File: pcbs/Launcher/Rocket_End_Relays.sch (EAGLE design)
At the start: 40 parts, among them IC2 LM2576T-ADJ, K4 LD105, K5 LD105, K6 LD105, K7 LD105, T1 BC547, T2 BC547, T3 BC547, T4 BC547, T5 BC547, U1 ARDUINO-MEGAPRO-5V, X1 1751248, X2 22-23-2041, X3 22-23-2021, X4 1751248, X5 22-23-2021

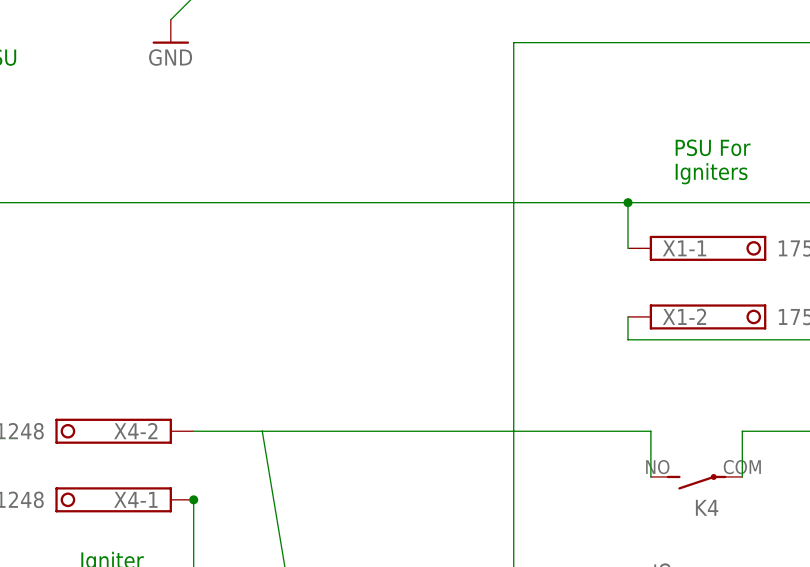
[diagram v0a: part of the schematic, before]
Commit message: * Moving relays in line a bit more * Added additional connector for Igniter battery, to give us more options * Rotated plugs
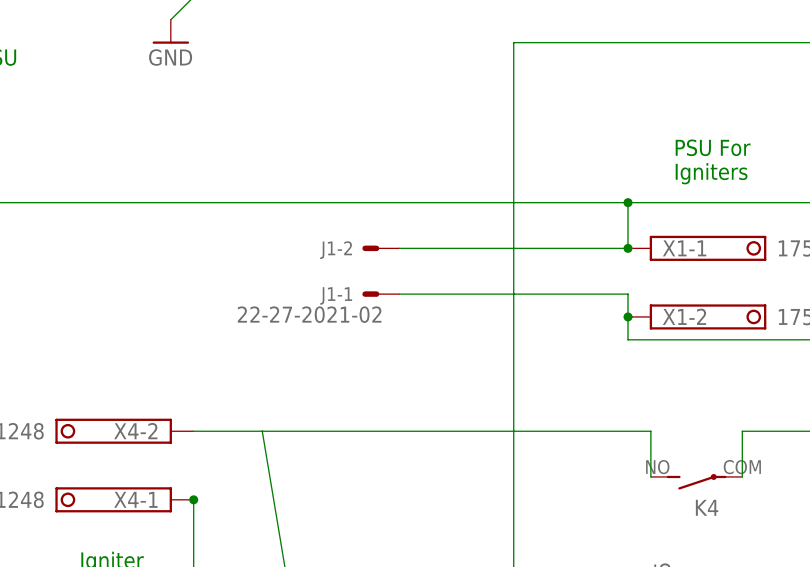
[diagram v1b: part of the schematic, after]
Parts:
- added J1: 22-27-2021-02, con-molex:22-27-2021-02
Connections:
- net N$29: now also J1-2.S
- net N$33: now also J1-1.S
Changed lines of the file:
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@@
 <part name="X4" library="con-phoenix-350" deviceset="1751248" device=""/>
 <part name="X5" library="con-molex" deviceset="22-23-2021" device=""/>
+<part name="J1" library="con-molex" deviceset="22-?-02" device="27-2021"/>
 </parts>
 <sheets>
@@
 <instance part="X5" gate="-1" x="-165.1" y="185.42" rot="R90"/>
 <instance part="X5" gate="-2" x="-162.56" y="185.42" rot="R90"/>
+<instance part="J1" gate="-1" x="-88.9" y="111.76" rot="R180"/>
+<instance part="J1" gate="-2" x="-88.9" y="116.84" rot="R180"/>
 </instances>
 <busses>
@@
 <wire x1="-22.86" y1="68.58" x2="-30.48" y2="68.58" width="0.1524" layer="91"/>
 <pinref part="X1" gate="-2" pin="K"/>
+<pinref part="J1" gate="-1" pin="S"/>
+<wire x1="-86.36" y1="111.76" x2="-60.96" y2="111.76" width="0.1524" layer="91"/>
+<wire x1="-60.96" y1="111.76" x2="-60.96" y2="109.22" width="0.1524" layer="91"/>
+<junction x="-60.96" y="109.22"/>
 </segment>
 <segment>
@@
 <pinref part="X1" gate="-1" pin="K"/>
 <junction x="-60.96" y="121.92"/>
-</segment>
-</net>
+<pinref part="J1" gate="-2" pin="S"/>
+<wire x1="-60.96" y1="116.84" x2="-86.36" y2="116.84" width="0.1524" layer="91"/>
+<junction x="-60.96" y="116.84"/>
+</segment>
+</net>

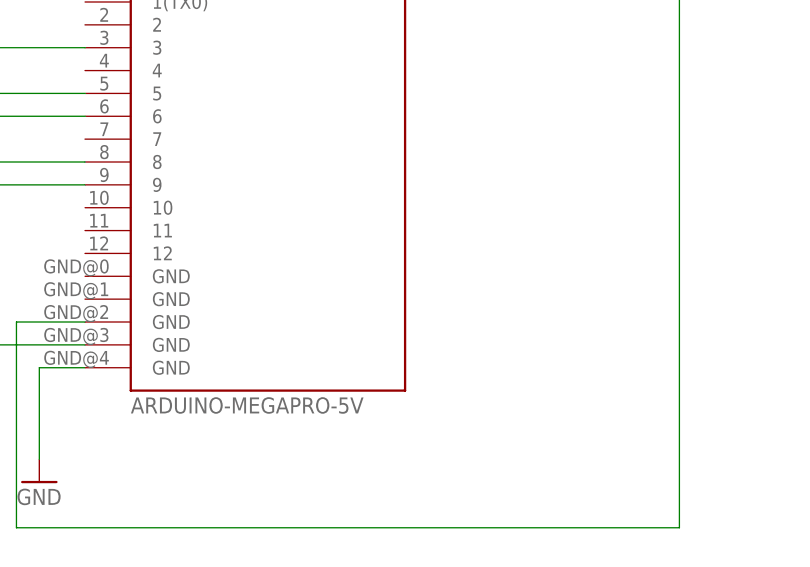
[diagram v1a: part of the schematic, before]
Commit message: * Adding my own updated library of sparkfun stuff.
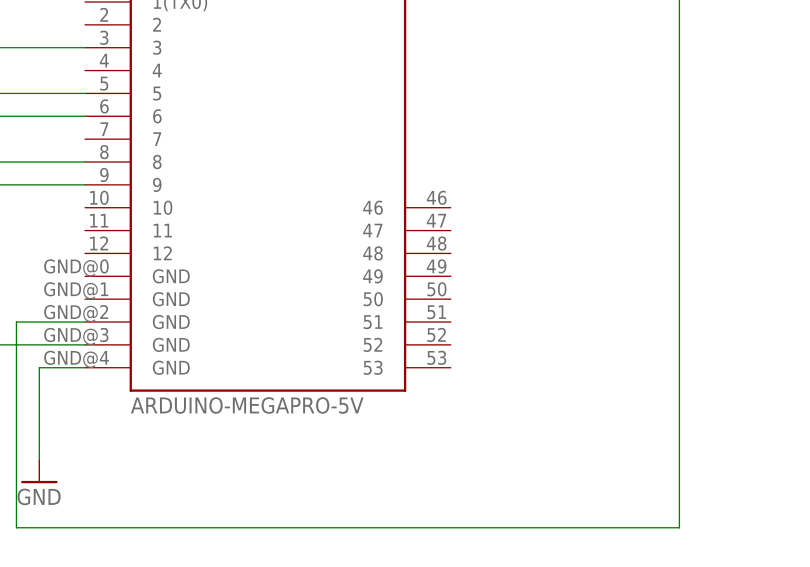
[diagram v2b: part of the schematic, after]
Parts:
- U1: device JoeMega_Ether_Edited:ARDUINO-MEGAPRO-5V -> Joe_SparkFun-Boards:ARDUINO-MEGAPRO-5V
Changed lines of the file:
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@@
 <layer number="56" name="wert" color="7" fill="1" visible="no" active="no"/>
 <layer number="57" name="tCAD" color="7" fill="1" visible="no" active="no"/>
+<layer number="59" name="tCarbon" color="7" fill="1" visible="no" active="no"/>
+<layer number="60" name="bCarbon" color="7" fill="1" visible="no" active="no"/>
 <layer number="90" name="Modules" color="5" fill="1" visible="yes" active="yes"/>
 <layer number="91" name="Nets" color="2" fill="1" visible="yes" active="yes"/>
@@
 <layer number="112" name="tSilk" color="7" fill="1" visible="yes" active="yes"/>
 <layer number="113" name="IDFDebug" color="7" fill="1" visible="yes" active="yes"/>
+<layer number="114" name="Badge_Outline" color="11" fill="1" visible="no" active="no"/>
 <layer number="116" name="Patch_BOT" color="9" fill="4" visible="yes" active="yes"/>
+<layer number="118" name="Rect_Pads" color="7" fill="1" visible="yes" active="yes"/>
 <layer number="121" name="_tsilk" color="7" fill="1" visible="yes" active="yes"/>
 <layer number="122" name="_bsilk" color="7" fill="1" visible="yes" active="yes"/>
@@
 <layer number="127" name="_tValues" color="7" fill="1" visible="yes" active="yes"/>
 <layer number="128" name="_bValues" color="7" fill="1" visible="yes" active="yes"/>
+<layer number="129" name="Mask" color="7" fill="1" visible="yes" active="yes"/>
 <layer number="131" name="tAdjust" color="7" fill="1" visible="yes" active="yes"/>
 <layer number="132" name="bAdjust" color="7" fill="1" visible="yes" active="yes"/>
@@
 <layer number="251" name="SMDround" color="12" fill="11" visible="no" active="no"/>
 <layer number="254" name="cooling" color="7" fill="1" visible="yes" active="yes"/>
+<layer number="255" name="routoute" color="7" fill="1" visible="yes" active="yes"/>
 </layers>
 <schematic xreflabel="%F%N/%S.%C%R" xrefpart="/%S.%C%R">
@@
 </classes>
 <parts>
-<part name="U1" library="JoeMega_Ether_Edited" deviceset="ARDUINO-MEGA" device="PRO-5V"/>
+<part name="U1" library="Joe_SparkFun-Boards" deviceset="ARDUINO-MEGA" device="PRO-5V"/>
 <part name="X2" library="con-molex" deviceset="22-23-2041" device=""/>
 <part name="R1" library="rcl" deviceset="R-US_" device="0204/7" value="15k"/>

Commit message: * making more space at PSU side of board for cut.
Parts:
- R13: device rcl:R-US_0204/5 -> resistor:R-US_0204/2V
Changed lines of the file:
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@@
 <part name="C4" library="rcl" deviceset="CPOL-US" device="E2-4" value="330uF 16V"/>
 <part name="L1" library="resistor" deviceset="L-US" device="TJ4-U1" value="100uH 3Amp"/>
-<part name="R13" library="rcl" deviceset="R-US_" device="0204/5" value="4.7k"/>
+<part name="R13" library="resistor" deviceset="R-US_" device="0204/2V" value="4.7k"/>
 <part name="R14" library="resistor" deviceset="R-US_" device="0207/7" value="1.5k"/>
 <part name="D5" library="diode" deviceset="1N5908" device="" value="1N5822"/>

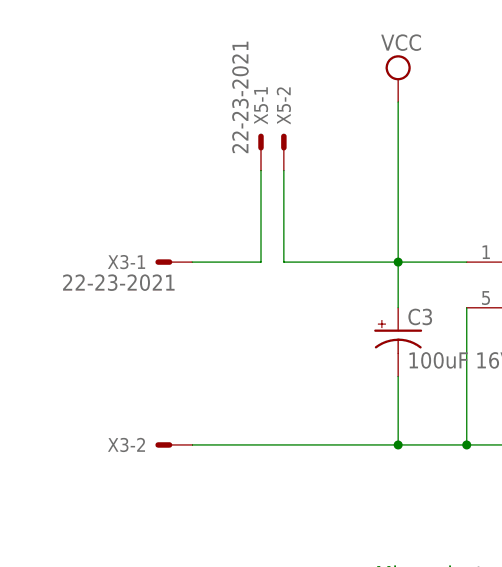
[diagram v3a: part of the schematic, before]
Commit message: * Removed some parts from Joe_Sparkfun-boards.lbf * A bit of a small tidy up on board relays
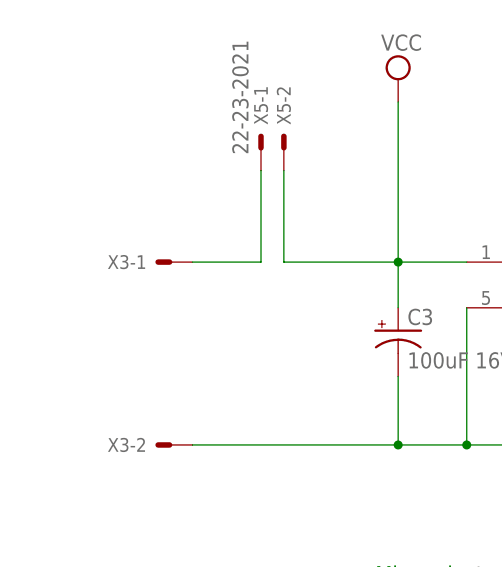
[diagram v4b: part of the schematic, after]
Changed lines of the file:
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@@
 <part name="GND1" library="supply1" deviceset="GND" device=""/>
 <part name="IC2" library="LM2576" deviceset="LM2576*" device="T-ADJ" value="LM2576T-ADJ"/>
-<part name="X3" library="con-molex" deviceset="22-23-2021" device=""/>
+<part name="X3" library="con-molex" deviceset="22-23-2021" device="" value=""/>
 <part name="C3" library="rcl" deviceset="CPOL-US" device="E2-4" value="100uF 16V"/>
 <part name="C4" library="rcl" deviceset="CPOL-US" device="E2-4" value="330uF 16V"/>
